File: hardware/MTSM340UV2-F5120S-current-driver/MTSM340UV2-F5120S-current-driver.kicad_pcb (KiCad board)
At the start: 2 copper layers, 122 x 81.5 mm, 229 parts, among them J1 LED0, J10 LED8, J11 LED9, J12 LED10, J13 LED11, J14 LED12, J15 LED13, J16 LED14, J17 LED15, J18 LED16, J19 LED17, J2 LED1, J20 LED18, J21 LED19, J22 LED20, J23 LED21, J24 LED22, J25 LED23, J26 FPC, J27 POWER, J3 LED2, J4 LED3, J5 LED4, J6 LED5, J7 LED6, J8 LED7, J9 ENABLE, SW1 RESET, SW2 GPIO0, U1 LM3407MY, U10 LM3407MY, U11 LM3407MY, U12 LM3407MY, U13 LM3407MY, U14 LM3407MY, U15 LM3407MY, U16 LM3407MY, U17 LM3407MY, U18 LM3407MY, U19 LM3407MY, U2 LM3407MY, U20 LM3407MY, U21 LM3407MY, U22 LM3407MY, U23 LM3407MY, U24 LM3407MY, U3 LM3407MY, U4 LM3407MY, U5 LM3407MY, U6 LM3407MY, U7 LM3407MY, U8 LM3407MY, U9 LM3407MY

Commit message: layout almost done
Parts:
- removed TP8: TestPoint, TestPoint:TestPoint_Pad_D1.0mm
- added D25: 12V, LED_SMD:LED_0603_1608Metric_Pad1.05x0.95mm_HandSolder, F.Cu at (71.1, 82.0)
- added D26: 5V, LED_SMD:LED_0603_1608Metric_Pad1.05x0.95mm_HandSolder, F.Cu at (71.0, 86.4)
- added H1: 12V, MountingHole:MountingHole_3.2mm_M3_DIN965_Pad_TopBottom, F.Cu at (164.5, 147.0)
- added H2: 12V, MountingHole:MountingHole_3.2mm_M3_DIN965_Pad_TopBottom, F.Cu at (164.5, 139.0)
- added H3: 12V, MountingHole:MountingHole_3.2mm_M3_DIN965_Pad_TopBottom, F.Cu at (164.5, 155.0)
- added H4: GND, MountingHole:MountingHole_3.2mm_M3_DIN965_Pad_TopBottom, F.Cu at (164.5, 84.0)
- added H5: GND, MountingHole:MountingHole_3.2mm_M3_DIN965_Pad_TopBottom, F.Cu at (164.5, 100.0)
- added H6: GND, MountingHole:MountingHole_3.2mm_M3_DIN965_Pad_TopBottom, F.Cu at (164.5, 92.0)
- added J28: UART, Connector_PinHeader_2.54mm:PinHeader_1x03_P2.54mm_Vertical, F.Cu at (50.9, 101.2)
- added R49: 1k, Resistor_SMD:R_0603_1608Metric_Pad0.98x0.95mm_HandSolder, F.Cu at (76.7, 92.6)
- added R50: 500, Resistor_SMD:R_0603_1608Metric_Pad0.98x0.95mm_HandSolder, F.Cu at (74.8, 82.0)
- added R51: 150, Resistor_SMD:R_0603_1608Metric_Pad0.98x0.95mm_HandSolder, F.Cu at (74.8, 86.4)
- C10: footprint Capacitor_SMD:C_0402_1005Metric -> Capacitor_SMD:C_0603_1608Metric_Pad1.08x0.95mm_HandSolder
- C11: footprint Capacitor_SMD:C_0402_1005Metric -> Capacitor_SMD:C_0805_2012Metric_Pad1.18x1.45mm_HandSolder
- C12: footprint Capacitor_SMD:C_0805_2012Metric -> Capacitor_SMD:C_0805_2012Metric_Pad1.18x1.45mm_HandSolder
- C8, C9: footprint Capacitor_SMD:C_0603_1608Metric -> Capacitor_SMD:C_0603_1608Metric_Pad1.08x0.95mm_HandSolder
- J26: footprint Connector_FFC-FPC:Molex_200528-0100_1x10-1MP_P1.00mm_Horizontal -> Connector_FFC-FPC:TE_1-84953-0_1x10-1MP_P1.0mm_Horizontal
- J27: value POWER -> Conn_01x05_Male; footprint Connector_BarrelJack:BarrelJack_CUI_PJ-063AH_Horizontal -> Connector_PinHeader_2.54mm:PinHeader_1x05_P2.54mm_Vertical
- L10, L11, L12, L13, L14, L15, L16, L17, L18, L19, L2, L20, L21, L22, L23, L24, L25, L3, L4, L5, L6, L7, L8, L9: footprint Inductor_SMD:L_1210_3225Metric_Pad1.42x2.65mm_HandSolder -> custom_lib:LQH3NPN
- moved J27 56.0 mm to (85.5, 92.4), turned to 180 degrees
- moved C11 46.8 mm to (52.7, 146.4), turned to 90 degrees
- moved C9 45.2 mm to (57.7, 149.1), turned to 180 degrees
- moved L1 44.9 mm to (51.7, 141.6), turned to 270 degrees
- moved MAX176321 42.2 mm to (56.7, 145.1), turned to 180 degrees
- moved C12 38.8 mm to (56.2, 140.6), turned to 180 degrees
- moved C8 38.1 mm to (60.2, 144.6), turned to 90 degrees
- moved C10 35.8 mm to (59.2, 141.1), turned to 90 degrees
- moved J9 13.9 mm to (70.7, 92.4), turned to 90 degrees
- moved SW2 11.2 mm to (65.6, 93.0), turned to 270 degrees
- moved SW1 7.11 mm to (65.6, 82.9), turned to 270 degrees
- moved J26 4.16 mm to (54.9, 88.8)
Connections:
- J27 pad 2: +12V -> +5V
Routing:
- net +12V: track 1075.8 -> 379.7 mm
- net PWM: track 0.00 -> 554.3 mm, vias 0 -> 25
- net ENABLE: track 0.00 -> 431.7 mm, vias 0 -> 17
- net +5V: track 13.2 -> 108.0 mm, vias 0 -> 5
- net RX: track 0.00 -> 23.8 mm
- net TX: track 0.00 -> 19.2 mm
- net Net-(J26-Pad4): track 0.00 -> 14.8 mm
- net Net-(J26-Pad3): track 0.00 -> 11.5 mm
- net Net-(C11-Pad1): track 1.61 -> 10.8 mm
- net Net-(C70-Pad2): track 0.00 -> 3.97 mm
- net GND: track 309.6 -> 313.1 mm
- net Net-(C11-Pad2): track 1.63 -> 2.74 mm
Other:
- copper layers 2 -> 4
- net class Default: trace_width 0.4 -> 0.3
- net class POWER: clearance 0.4 -> 0.2
- board text added: "ENABLE"
- board text added: "FLASH"
- board text added: "GND"
- board text added: "RESET"
- board text added: "RX"
- board text added: "TX"

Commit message: layout done
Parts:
- added H10: MountingHole, MountingHole:MountingHole_3.2mm_M3_DIN965, F.Cu at (141.1, 156.2)
- added H7: MountingHole, MountingHole:MountingHole_3.2mm_M3_DIN965, F.Cu at (52.1, 156.2)
- added H8: MountingHole, MountingHole:MountingHole_3.2mm_M3_DIN965, F.Cu at (59.1, 105.2)
- added H9: MountingHole, MountingHole:MountingHole_3.2mm_M3_DIN965, F.Cu at (141.1, 83.2)
- moved C59 0.81 mm to (114.7, 158.9)
- moved R36 0.51 mm to (111.0, 158.9)
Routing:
- net +12V: track 379.7 -> 1058.8 mm, vias 0 -> 1
- net ENABLE: track 431.7 -> 574.9 mm, vias 17 -> 24
- net GND: track 313.1 -> 323.3 mm, vias 0 -> 1
- net Net-(C46-Pad2): track 0.00 -> 3.56 mm
- net +5V: track 108.0 -> 110.4 mm
- net Net-(D26-Pad2): track 0.00 -> 2.01 mm
- net Net-(D25-Pad2): track 0.00 -> 1.93 mm
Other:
- net class Default: trace_width 0.3 -> 0.25
- net class POWER: clearance 0.2 -> 0.4
- board text added: "12V"
- board text added: "5V"
- board text added: "PWM"

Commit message: ready for order
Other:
- board text added: "uven 3.0"

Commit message: with step export
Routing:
- net PWM: track 554.2 -> 551.8 mm

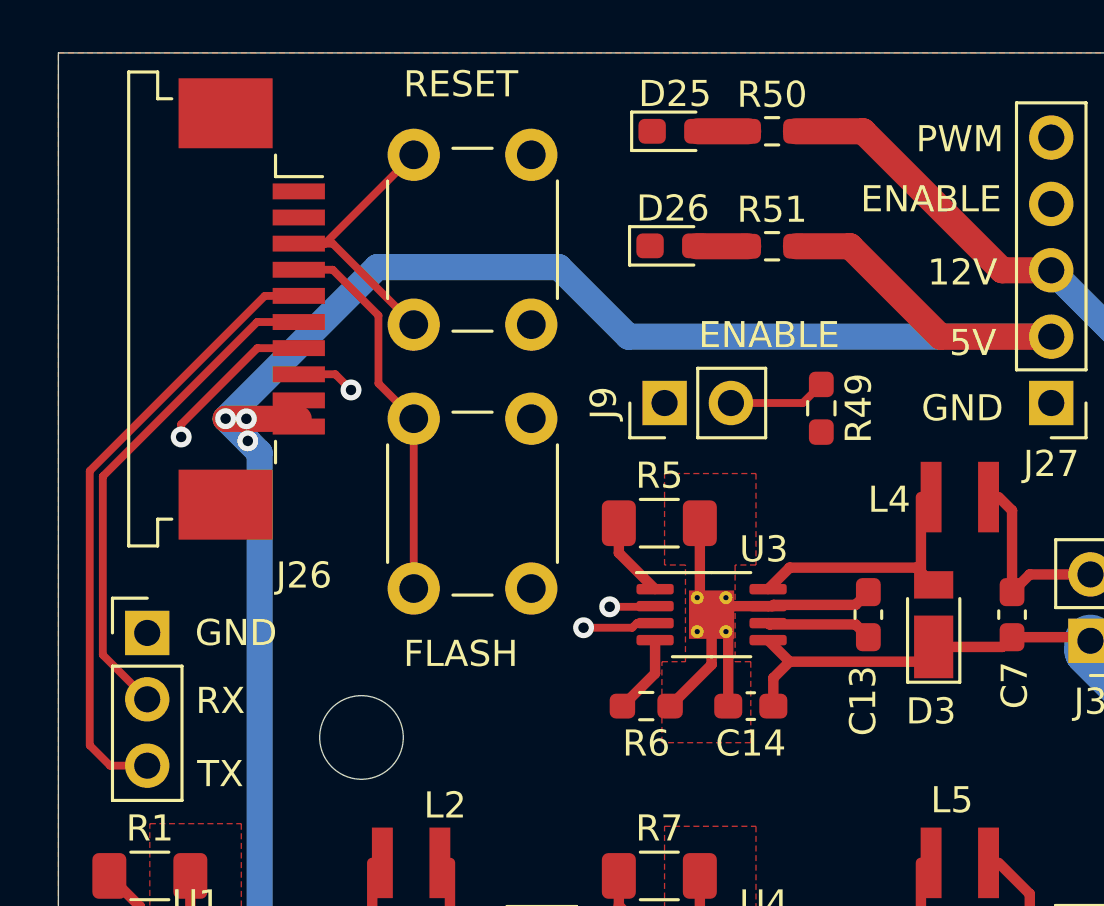
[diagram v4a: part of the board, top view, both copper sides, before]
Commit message: with correct fpc connector and pullup on enable
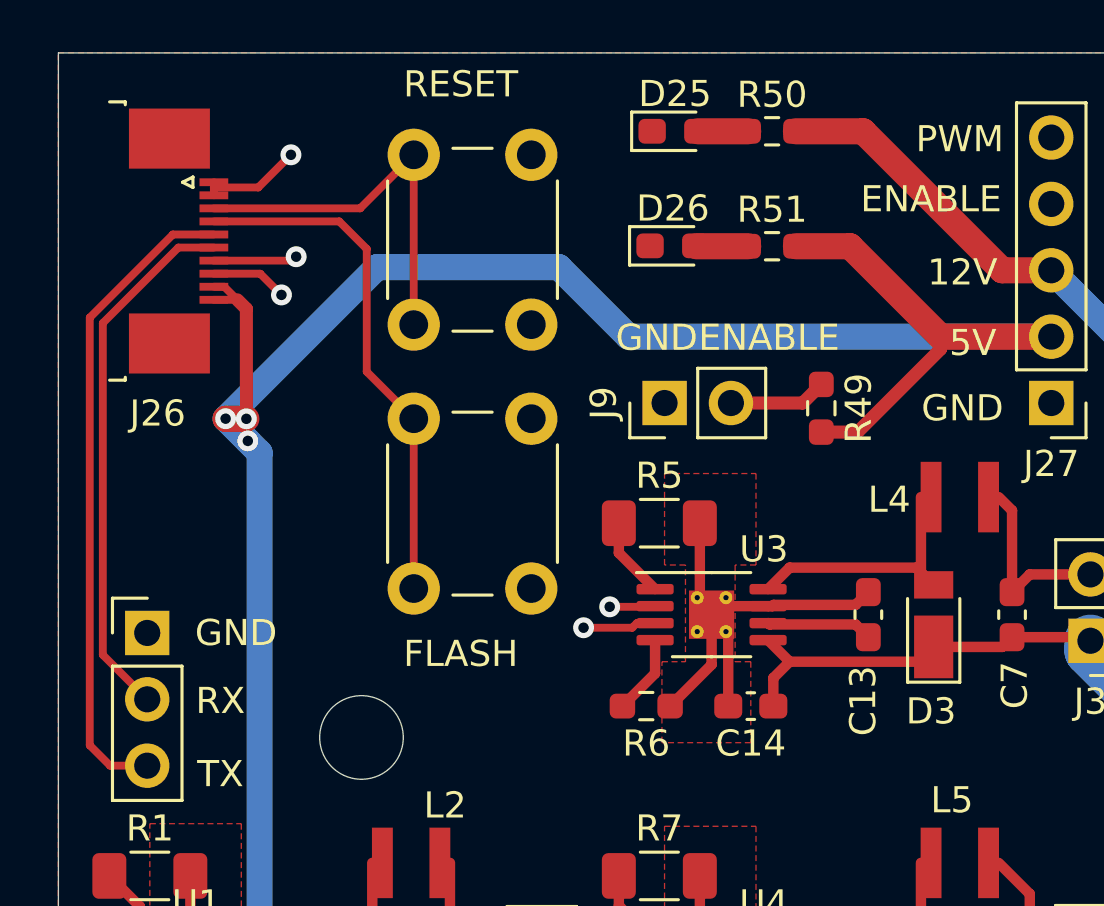
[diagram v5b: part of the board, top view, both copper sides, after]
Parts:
- J26: footprint Connector_FFC-FPC:TE_1-84953-0_1x10-1MP_P1.0mm_Horizontal -> Connector_FFC-FPC:TE_1-1734839-0_1x10-1MP_P0.5mm_Horizontal
- moved J26 3.82 mm to (52.1, 86.2)
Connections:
- R49 pad 2: GND -> +5V
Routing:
- net +5V: track 110.4 -> 120.5 mm
- net Net-(J26-Pad4): track 14.8 -> 20.0 mm
- net PWM: track 551.8 -> 556.3 mm
- net Net-(J26-Pad3): track 11.5 -> 15.0 mm
- net TX: track 19.2 -> 20.6 mm
- net RX: track 23.8 -> 25.0 mm
- net GND: track 323.3 -> 324.3 mm, vias 1 -> 2
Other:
- net class Default: trace_width 0.25 -> 0.3
